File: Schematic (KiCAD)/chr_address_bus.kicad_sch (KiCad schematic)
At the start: 40 parts

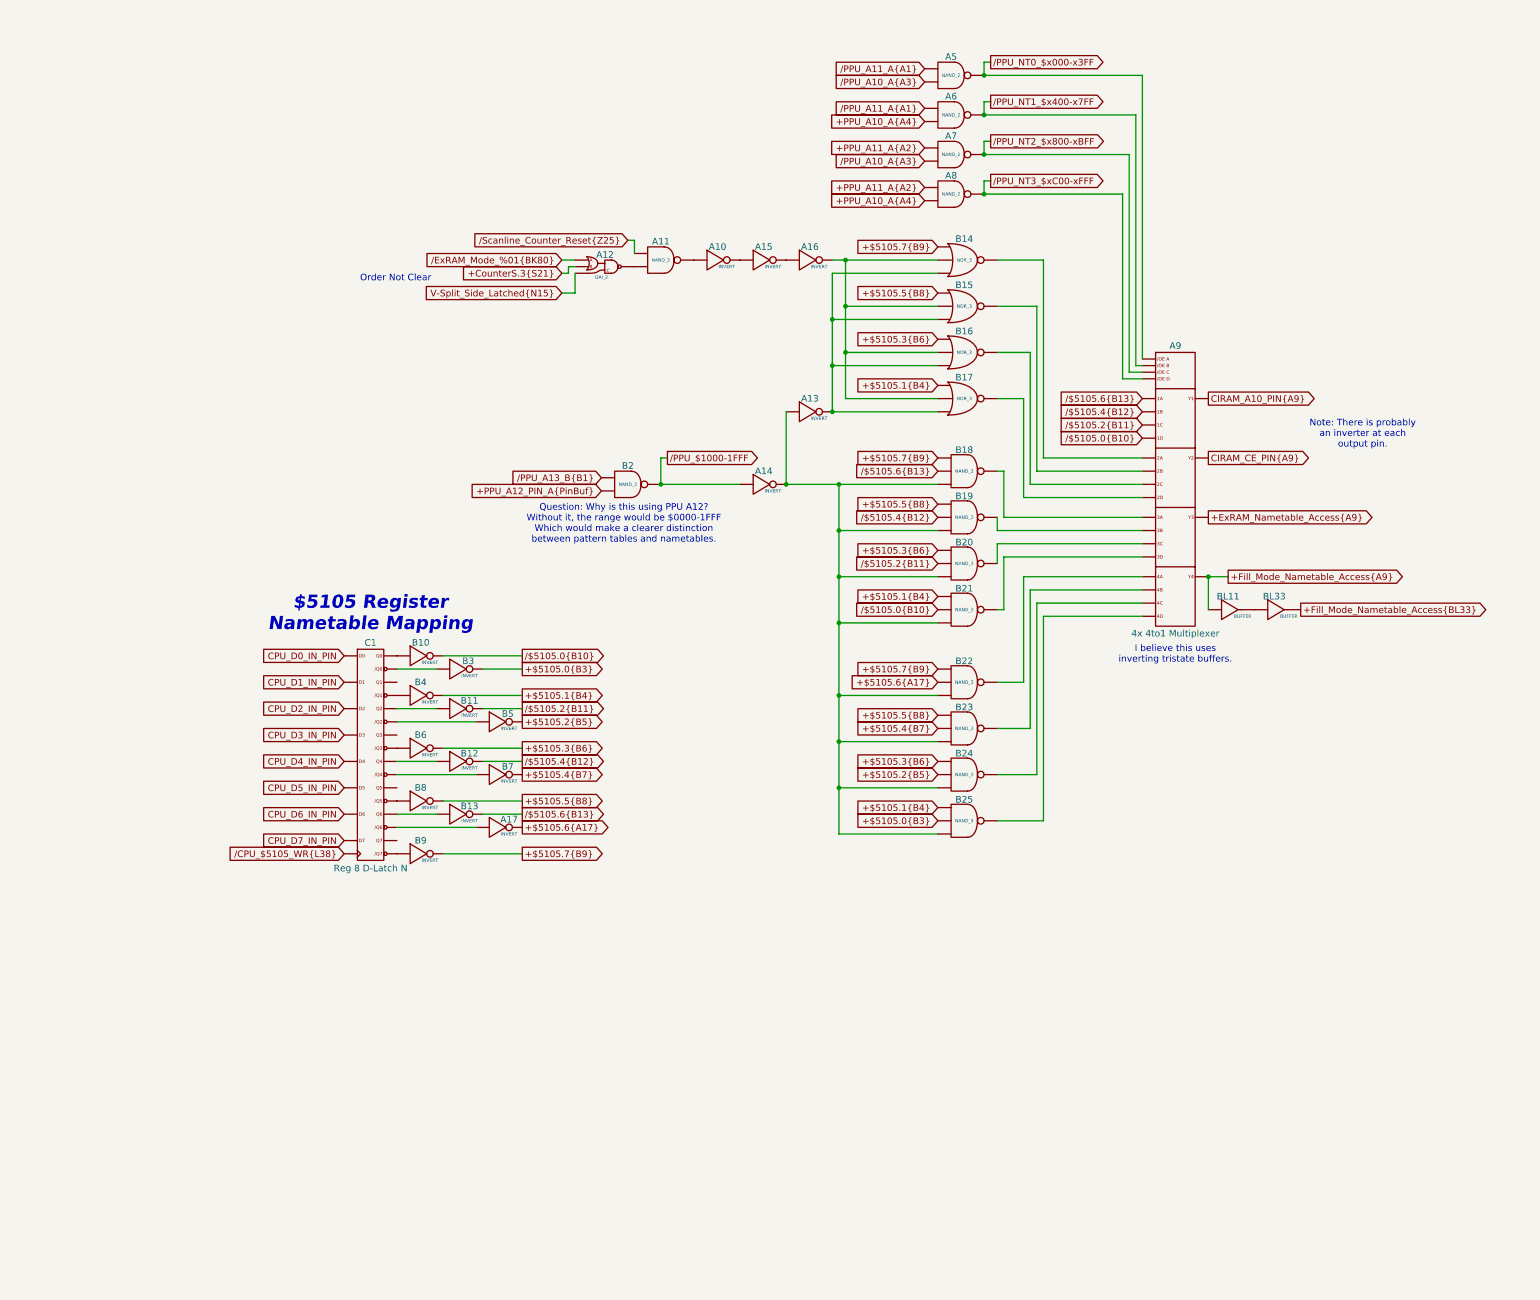
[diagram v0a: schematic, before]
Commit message: Schematic Updates:  - Added all 10-bit CHR banking registers $5120 - $512B, including where all 10 bits come from when written.  - Added 8-bit CHR bank register $5202, which is the bank used when rendering the V-Split region.    + V-Split seems to always be 8-bit, 8kB bank regardless of CHR mode.  The wiki doesn't say that and I don't know for sure.  - Added decoding logic that activates the correct CHR bank for CHR A10, A11, A12 (corresponding to columns AV, AW, AX).  - Noted, AX15 activates $5202 CHR Bank for V-Split region.  AX16 activates CHR Bank from data stored in ExRAM for extended attributes.  Therefore, AX15 driven by AT1 High means we specifically are in v-split region, and not extended attribute mode.  With this knowledge, backtracking up the chain from AT1 to N14 sheds very useful insight what the 3-bit shift register at N11/N12/N13 is doing.  We now know that N14 goes low specifically for pattern table fetches when rendering the V-split region, and does not appear dual-purposed for extended attribute fetch sequencing.  This may seem rather subtle or unimportant, but it is a good advancement for higher level understanding what that mysterious shift register might be doing.
SVG Trace Updates:
 - Registers $5120, 5121, 5122, 5123 (first 4 CHR bank register), the outputs were labeled in reverse order.
 - Register $5130 (highest CHR bank bits), the outputs were labeled with backwards polarity.  The error was not having taken into account that the CPU data bus input to the latches came already inverted to begin with.
 - Still wrong: Cell AV7, 2-input NAND gate.  One of the inputs is missing and it logically should be driven by AS19 like the 4 cells to its direct right.  I can't quite make out how it makes that connection.
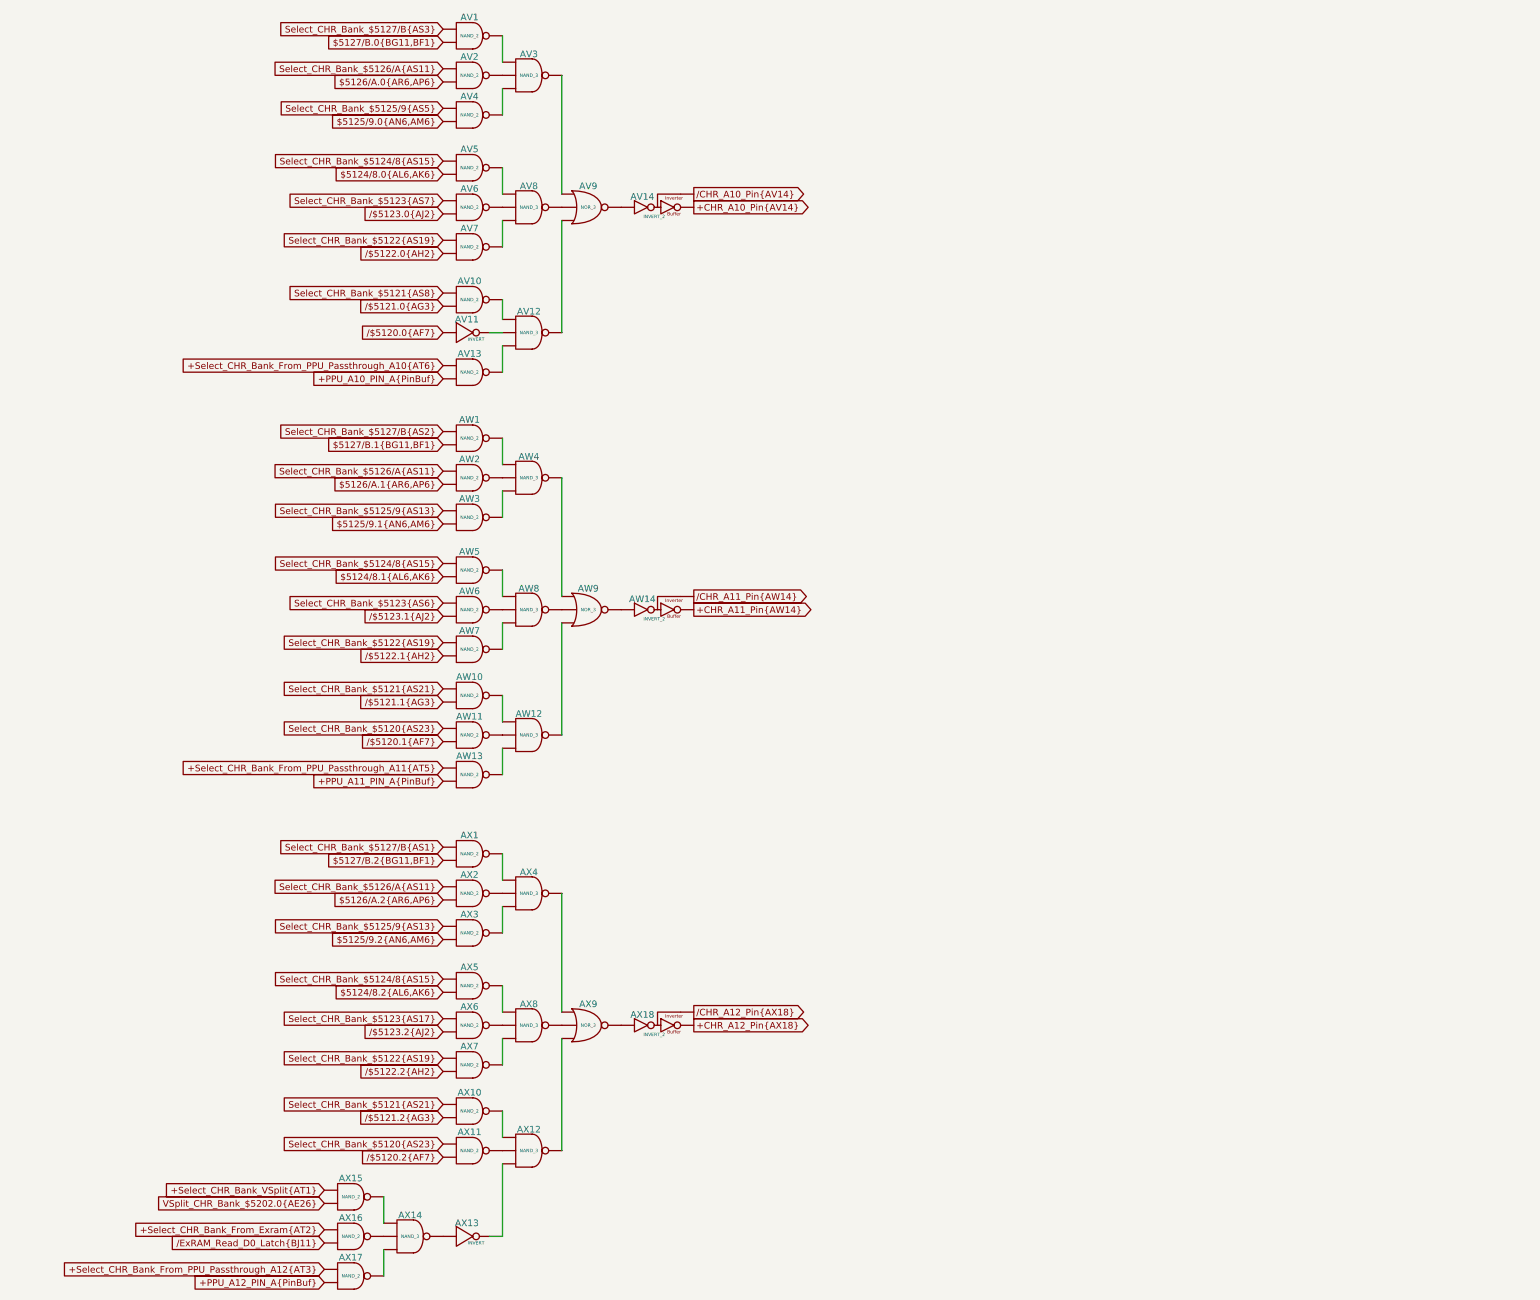
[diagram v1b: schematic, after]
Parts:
- removed A10, A13, A14, A15, A16, A17, B10, B11, B12, B13, B3, B4, B5, B6, B7, B8, B9: INVERT, symbol MMC5:INVERT
- removed A11, A5, A6, A7, A8, B2: NAND_2, symbol MMC5:NAND_2
- removed A12: OAI_2, symbol MMC5:OAI_2
- removed A9: 4x 4to1 Multiplexer, symbol MMC5:Multiplexer_4x4to1
- removed B14, B15, B16, B17: NOR_3, symbol MMC5:NOR_3
- removed B18, B19, B20, B21, B22, B23, B24, B25: NAND_3, symbol MMC5:NAND_3
- removed BL11, BL33: BUFFER, symbol MMC5:BUFFER
- removed C1: Reg 8 D-Latch N, symbol MMC5:Reg_8_D-Latch_N
- added AV1, AV10, AV13, AV2, AV4, AV5, AV6, AV7, AW1, AW10, AW11, AW13, AW2, AW3, AW5, AW6, AW7, AX1, AX10, AX11, AX15, AX16, AX17, AX2, AX3, AX5, AX6, AX7: NAND_2, symbol MMC5:NAND_2
- added AV11, AX13: INVERT, symbol MMC5:INVERT
- added AV12, AV3, AV8, AW12, AW4, AW8, AX12, AX14, AX4, AX8: NAND_3, symbol MMC5:NAND_3
- added AV14, AW14, AX18: INVERT_2, symbol MMC5:INVERT_2
- added AV9, AW9, AX9: NOR_3, symbol MMC5:NOR_3
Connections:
- net +PPU_A12_PIN_A{PinBuf}: now also AX17. (X)
- new net: AX7. (X), AX8. (X)
- new net: AV1. (X), AV3. (X)
- new net: AW5. (X), AW8. (X)
- new net: AW12. (X), AW13. (X)
- new net: AX4. (X), AX9. (X)
- new net: AX3. (X), AX4. (X)
- new net: AX1. (X), AX4. (X)
- new net: AX2. (X), AX4. (X)
- new net: AW14. (X), AW9. (X)
- new net: AW7. (X), AW8. (X)
- new net: AX5. (X), AX8. (X)
- new net: AX14. (X), AX16. (X)
- new net: AX13. (X), AX14. (X)
- new net: AX14. (X), AX15. (X)
- new net: AX14. (X), AX17. (X)
- new net: AV12. (X), AV9. (X)
- new net: AV8. (X), AV9. (X)
- new net: AV14. (X), AV9. (X)
- new net: AV3. (X), AV9. (X)
- new net: AX11. (X), AX12. (X)
- new net: AX12. (X), AX9. (X)
- new net: AX12. (X), AX13. (X)
- new net: AX10. (X), AX12. (X)
- new net: AV10. (X), AV12. (X)
- new net: AV11. (X), AV12. (X)
- new net: AV12. (X), AV13. (X)
- new net: AW12. (X), AW9. (X)
- new net: AW4. (X), AW9. (X)
- new net: AW8. (X), AW9. (X)
- new net: AW10. (X), AW12. (X)
- new net: AX8. (X), AX9. (X)
- new net: AX18. (X), AX9. (X)
- new net: AV7. (X), AV8. (X)
- new net: AV5. (X), AV8. (X)
- new net: AV6. (X), AV8. (X)
- new net: AV2. (X), AV3. (X)
- new net: AW11. (X), AW12. (X)
- new net: AX6. (X), AX8. (X)
- new net: AW2. (X), AW4. (X)
- new net: AW3. (X), AW4. (X)
- new net: AV3. (X), AV4. (X)
- new net: AW1. (X), AW4. (X)
- new net: AW6. (X), AW8. (X)
- new net $5124/8.0{AL6,AK6}: AV5. (X)
- new net $5124/8.1{AL6,AK6}: AW5. (X)
- new net $5124/8.2{AL6,AK6}: AX5. (X)
- new net $5125/9.0{AN6,AM6}: AV4. (X)
- new net $5125/9.1{AN6,AM6}: AW3. (X)
- new net $5125/9.2{AN6,AM6}: AX3. (X)
- new net $5126/A.0{AR6,AP6}: AV2. (X)
- new net $5126/A.1{AR6,AP6}: AW2. (X)
- new net $5126/A.2{AR6,AP6}: AX2. (X)
- new net $5127/B.0{BG11,BF1}: AV1. (X)
- new net $5127/B.1{BG11,BF1}: AW1. (X)
- new net $5127/B.2{BG11,BF1}: AX1. (X)
- new net +CHR_A10_Pin{AV14}: AV14. (X)
- new net +CHR_A11_Pin{AW14}: AW14. (X)
- new net +CHR_A12_Pin{AX18}: AX18. (X)
- new net +PPU_A10_PIN_A{PinBuf}: AV13. (X)
- new net +PPU_A11_PIN_A{PinBuf}: AW13. (X)
- new net +Select_CHR_Bank_From_Exram{AT2}: AX16. (X)
- new net +Select_CHR_Bank_From_PPU_Passthrough_A10{AT6}: AV13. (X)
- new net +Select_CHR_Bank_From_PPU_Passthrough_A11{AT5}: AW13. (X)
- new net +Select_CHR_Bank_From_PPU_Passthrough_A12{AT3}: AX17. (X)
- new net +Select_CHR_Bank_VSplit{AT1}: AX15. (X)
- new net Select_CHR_Bank_$5120{AS23}: AW11. (X), AX11. (X)
- new net Select_CHR_Bank_$5121{AS21}: AW10. (X), AX10. (X)
- new net Select_CHR_Bank_$5121{AS8}: AV10. (X)
- new net Select_CHR_Bank_$5122{AS19}: AV7. (X), AW7. (X), AX7. (X)
- new net Select_CHR_Bank_$5123{AS17}: AX6. (X)
- new net Select_CHR_Bank_$5123{AS6}: AW6. (X)
- new net Select_CHR_Bank_$5123{AS7}: AV6. (X)
- new net Select_CHR_Bank_$5124/8{AS15}: AV5. (X), AW5. (X), AX5. (X)
- new net Select_CHR_Bank_$5125/9{AS13}: AW3. (X), AX3. (X)
- new net Select_CHR_Bank_$5125/9{AS5}: AV4. (X)
- new net Select_CHR_Bank_$5126/A{AS11}: AV2. (X), AW2. (X), AX2. (X)
- new net Select_CHR_Bank_$5127/B{AS1}: AX1. (X)
- new net Select_CHR_Bank_$5127/B{AS2}: AW1. (X)
- new net Select_CHR_Bank_$5127/B{AS3}: AV1. (X)
- new net VSplit_CHR_Bank_$5202.0{AE26}: AX15. (X)
- new net /$5120.0{AF7}: AV11. (X)
- new net /$5120.1{AF7}: AW11. (X)
- new net /$5120.2{AF7}: AX11. (X)
- new net /$5121.0{AG3}: AV10. (X)
- new net /$5121.1{AG3}: AW10. (X)
- new net /$5121.2{AG3}: AX10. (X)
- new net /$5122.0{AH2}: AV7. (X)
- new net /$5122.1{AH2}: AW7. (X)
- new net /$5122.2{AH2}: AX7. (X)
- new net /$5123.0{AJ2}: AV6. (X)
- new net /$5123.1{AJ2}: AW6. (X)
- new net /$5123.2{AJ2}: AX6. (X)
- new net /CHR_A10_Pin{AV14}: AV14. (X)
- new net /CHR_A11_Pin{AW14}: AW14. (X)
- new net /CHR_A12_Pin{AX18}: AX18. (X)
- new net /ExRAM_Read_D0_Latch{BJ11}: AX16. (X)
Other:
- note removed: "$5105 Register Nametable Mapping"
- note removed: "I believe this uses inverting tristate buffers."
- note removed: "Note: There is probably an inverter at each output pin."
- note removed: "Order Not Clear"
- note removed: "Question: Why is this using PPU A12? Without it, the range would be $0000-1FFF Which would make a clearer distinction between pattern tables and nametables."
